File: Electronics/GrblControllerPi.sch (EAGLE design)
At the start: 21 parts, among them IC1 ATMEGA168-20P, SW1 SPST_TACT-EVQQ2

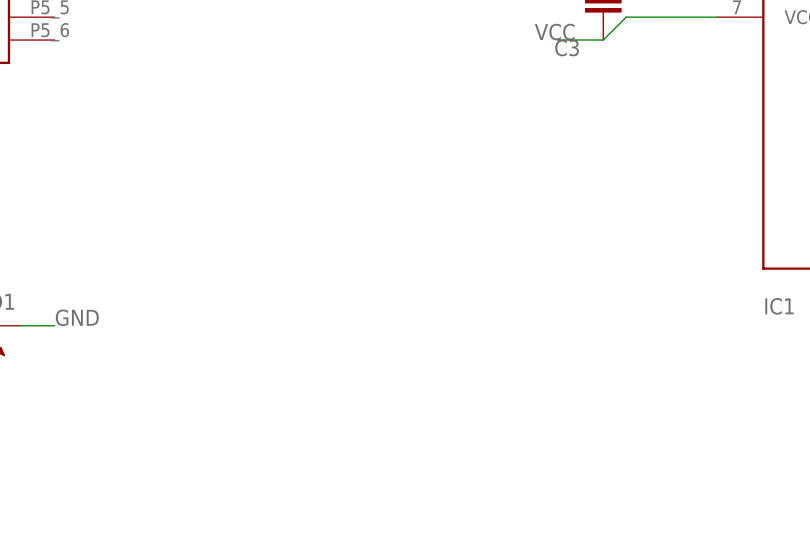
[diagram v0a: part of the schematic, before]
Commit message: Added Stepper Driver
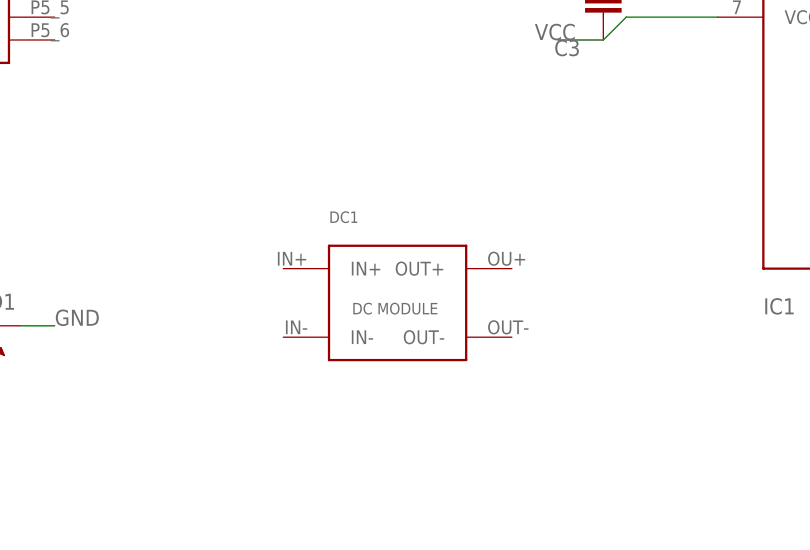
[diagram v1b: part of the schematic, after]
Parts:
- added DC1: (no value), OpenHardware.co.za:BUCKBOOST
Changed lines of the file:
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@@
 <setting verticaltext="up"/>
 </settings>
-<grid distance="0.05" unitdist="inch" unit="inch" style="lines" multiple="1" display="no" altdistance="0.01" altunitdist="inch" altunit="inch"/>
+<grid distance="0.1" unitdist="inch" unit="inch" style="lines" multiple="1" display="no" altdistance="0.01" altunitdist="inch" altunit="inch"/>
 <layers>
-<layer number="1" name="Top" color="4" fill="1" visible="yes" active="no"/>
-<layer number="16" name="Bottom" color="1" fill="1" visible="yes" active="no"/>
-<layer number="17" name="Pads" color="2" fill="1" visible="yes" active="no"/>
-<layer number="18" name="Vias" color="2" fill="1" visible="yes" active="no"/>
-<layer number="19" name="Unrouted" color="6" fill="1" visible="yes" active="no"/>
-<layer number="20" name="Dimension" color="15" fill="1" visible="yes" active="no"/>
-<layer number="21" name="tPlace" color="7" fill="1" visible="yes" active="no"/>
-<layer number="22" name="bPlace" color="7" fill="1" visible="yes" active="no"/>
-<layer number="23" name="tOrigins" color="15" fill="1" visible="yes" active="no"/>
-<layer number="24" name="bOrigins" color="15" fill="1" visible="yes" active="no"/>
-<layer number="25" name="tNames" color="7" fill="1" visible="yes" active="no"/>
-<layer number="26" name="bNames" color="7" fill="1" visible="yes" active="no"/>
-<layer number="27" name="tValues" color="7" fill="1" visible="yes" active="no"/>
-<layer number="28" name="bValues" color="7" fill="1" visible="yes" active="no"/>
+<layer number="1" name="Top" color="4" fill="1" visible="no" active="no"/>
+<layer number="2" name="Route2" color="1" fill="3" visible="no" active="no"/>
+<layer number="3" name="Route3" color="4" fill="3" visible="no" active="no"/>
+<layer number="4" name="Route4" color="1" fill="4" visible="no" active="no"/>
+<layer number="5" name="Route5" color="4" fill="4" visible="no" active="no"/>
+<layer number="6" name="Route6" color="1" fill="8" visible="no" active="no"/>
+<layer number="7" name="Route7" color="4" fill="8" visible="no" active="no"/>
+<layer number="8" name="Route8" color="1" fill="2" visible="no" active="no"/>
+<layer number="9" name="Route9" color="4" fill="2" visible="no" active="no"/>
+<layer number="10" name="Route10" color="1" fill="7" visible="no" active="no"/>
+<layer number="11" name="Route11" color="4" fill="7" visible="no" active="no"/>
+<layer number="12" name="Route12" color="1" fill="5" visible="no" active="no"/>
+<layer number="13" name="Route13" color="4" fill="5" visible="no" active="no"/>
+<layer number="14" name="Route14" color="1" fill="6" visible="no" active="no"/>
+<layer number="15" name="Route15" color="4" fill="6" visible="no" active="no"/>
+<layer number="16" name="Bottom" color="1" fill="1" visible="no" active="no"/>
+<layer number="17" name="Pads" color="2" fill="1" visible="no" active="no"/>
+<layer number="18" name="Vias" color="2" fill="1" visible="no" active="no"/>
+<layer number="19" name="Unrouted" color="6" fill="1" visible="no" active="no"/>
+<layer number="20" name="Dimension" color="15" fill="1" visible="no" active="no"/>
+<layer number="21" name="tPlace" color="7" fill="1" visible="no" active="no"/>
+<layer number="22" name="bPlace" color="7" fill="1" visible="no" active="no"/>
+<layer number="23" name="tOrigins" color="15" fill="1" visible="no" active="no"/>
+<layer number="24" name="bOrigins" color="15" fill="1" visible="no" active="no"/>
+<layer number="25" name="tNames" color="7" fill="1" visible="no" active="no"/>
+<layer number="26" name="bNames" color="7" fill="1" visible="no" active="no"/>
+<layer number="27" name="tValues" color="7" fill="1" visible="no" active="no"/>
+<layer number="28" name="bValues" color="7" fill="1" visible="no" active="no"/>
 <layer number="29" name="tStop" color="7" fill="3" visible="no" active="no"/>
 <layer number="30" name="bStop" color="7" fill="6" visible="no" active="no"/>
@@
 <layer number="35" name="tGlue" color="7" fill="4" visible="no" active="no"/>
 <layer number="36" name="bGlue" color="7" fill="5" visible="no" active="no"/>
-<layer number="37" name="tTest" color="7" fill="1" visible="yes" active="no"/>
-<layer number="38" name="bTest" color="7" fill="1" visible="yes" active="no"/>
+<layer number="37" name="tTest" color="7" fill="1" visible="no" active="no"/>
+<layer number="38" name="bTest" color="7" fill="1" visible="no" active="no"/>
 <layer number="39" name="tKeepout" color="4" fill="11" visible="no" active="no"/>
 <layer number="40" name="bKeepout" color="1" fill="11" visible="no" active="no"/>
@@
 <layer number="44" name="Drills" color="7" fill="1" visible="no" active="no"/>
 <layer number="45" name="Holes" color="7" fill="1" visible="no" active="no"/>
-<layer number="46" name="Milling" color="3" fill="1" visible="yes" active="no"/>
-<layer number="47" name="Measures" color="7" fill="1" visible="yes" active="no"/>
-<layer number="48" name="Document" color="7" fill="1" visible="yes" active="no"/>
-<layer number="49" name="Reference" color="7" fill="1" visible="yes" active="no"/>
-<layer number="50" name="dxf" color="7" fill="1" visible="yes" active="no"/>
-<layer number="51" name="tDocu" color="7" fill="1" visible="yes" active="no"/>
-<layer number="52" name="bDocu" color="7" fill="1" visible="yes" active="no"/>
-<layer number="53" name="tGND_GNDA" color="7" fill="9" visible="yes" active="no"/>
-<layer number="54" name="bGND_GNDA" color="1" fill="9" visible="yes" active="no"/>
-<layer number="56" name="wert" color="7" fill="1" visible="yes" active="no"/>
-<layer number="57" name="tCAD" color="7" fill="1" visible="yes" active="no"/>
+<layer number="46" name="Milling" color="3" fill="1" visible="no" active="no"/>
+<layer number="47" name="Measures" color="7" fill="1" visible="no" active="no"/>
+<layer number="48" name="Document" color="7" fill="1" visible="no" active="no"/>
+<layer number="49" name="Reference" color="7" fill="1" visible="no" active="no"/>
+<layer number="50" name="dxf" color="7" fill="1" visible="no" active="no"/>
+<layer number="51" name="tDocu" color="7" fill="1" visible="no" active="no"/>
+<layer number="52" name="bDocu" color="7" fill="1" visible="no" active="no"/>
+<layer number="53" name="tGND_GNDA" color="7" fill="9" visible="no" active="no"/>
+<layer number="54" name="bGND_GNDA" color="1" fill="9" visible="no" active="no"/>
+<layer number="56" name="wert" color="7" fill="1" visible="no" active="no"/>
+<layer number="57" name="tCAD" color="7" fill="1" visible="no" active="no"/>
 <layer number="91" name="Nets" color="2" fill="1" visible="yes" active="yes"/>
 <layer number="92" name="Busses" color="1" fill="1" visible="yes" active="yes"/>
@@
 <layer number="251" name="SMDround" color="12" fill="11" visible="no" active="no"/>
 <layer number="254" name="cooling" color="7" fill="1" visible="yes" active="yes"/>
+<layer number="255" name="OHSILK" color="7" fill="1" visible="yes" active="yes"/>
 </layers>
 <schematic xreflabel="%F%N/%S.%C%R" xrefpart="/%S.%C%R">
@@
 <part name="R4" library="dp_devices" deviceset="RESISTOR" device="-1206" value="1K"/>
 <part name="LED1" library="adafruit" deviceset="LED" device="CHIPLED_1206"/>
+<part name="DC1" library="OpenHardware.co.za" deviceset="BUCKBOOST" device=""/>
 </parts>
 <sheets>
@@
 <instance part="R4" gate="G$1" x="40.64" y="-29.21" rot="R180"/>
 <instance part="LED1" gate="G$1" x="49.53" y="-29.21" rot="R90"/>
+<instance part="DC1" gate="G$1" x="157.48" y="-48.26"/>
 </instances>
 <busses>

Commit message: Minor Tweaks to hardware + Added GrblpiB+ boards
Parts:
- removed DC1: (no value), OpenHardware.co.za:BUCKBOOST
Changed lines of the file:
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@@
 <part name="R4" library="dp_devices" deviceset="RESISTOR" device="-1206" value="1K"/>
 <part name="LED1" library="adafruit" deviceset="LED" device="CHIPLED_1206"/>
-<part name="DC1" library="OpenHardware.co.za" deviceset="BUCKBOOST" device=""/>
 </parts>
 <sheets>
@@
 <instance part="R4" gate="G$1" x="40.64" y="-29.21" rot="R180"/>
 <instance part="LED1" gate="G$1" x="49.53" y="-29.21" rot="R90"/>
-<instance part="DC1" gate="G$1" x="157.48" y="-48.26"/>
 </instances>
 <busses>
